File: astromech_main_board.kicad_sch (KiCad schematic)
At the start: 75 parts, among them IC1 MAX11645EUA+, J1 Screw_Terminal_01x02, J10 MOT_HEAD, J11 MOT_RIGHT, J12 RC UART RX, J13 MOT_LEFT, J14 Qwiic, J15 Qwiic, J2 Screw_Terminal_01x02, J3 Screw_Terminal_01x02, J4 IO_XPAND, J5 LEDs, J6 SCREEN, J7 DPAD, J8 RST_BTN, J9 I2C, U1 TCA9554DW, U10 LS7366R, U11 LS7366R, U2 TCA9554DW, U3 NCP1117-3.3_SOT223, U4 NCP1117-5.0_TO252, U5 TXB0108PW, U6 TXB0108PW, U7 TCA9517ADGK, U8 74HC14, U9 LS7366R, Y1 Crystal

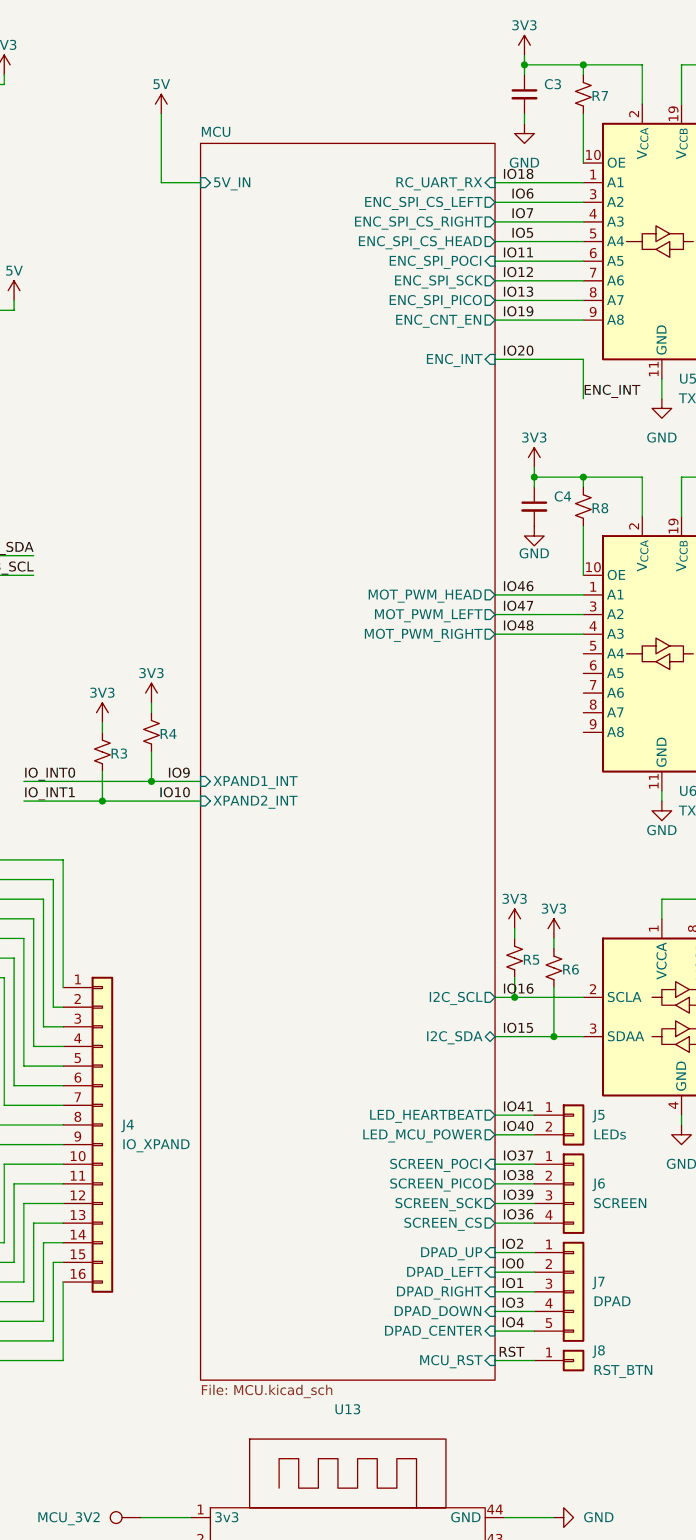
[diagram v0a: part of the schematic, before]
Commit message: Removed Block
- Everything should be on page
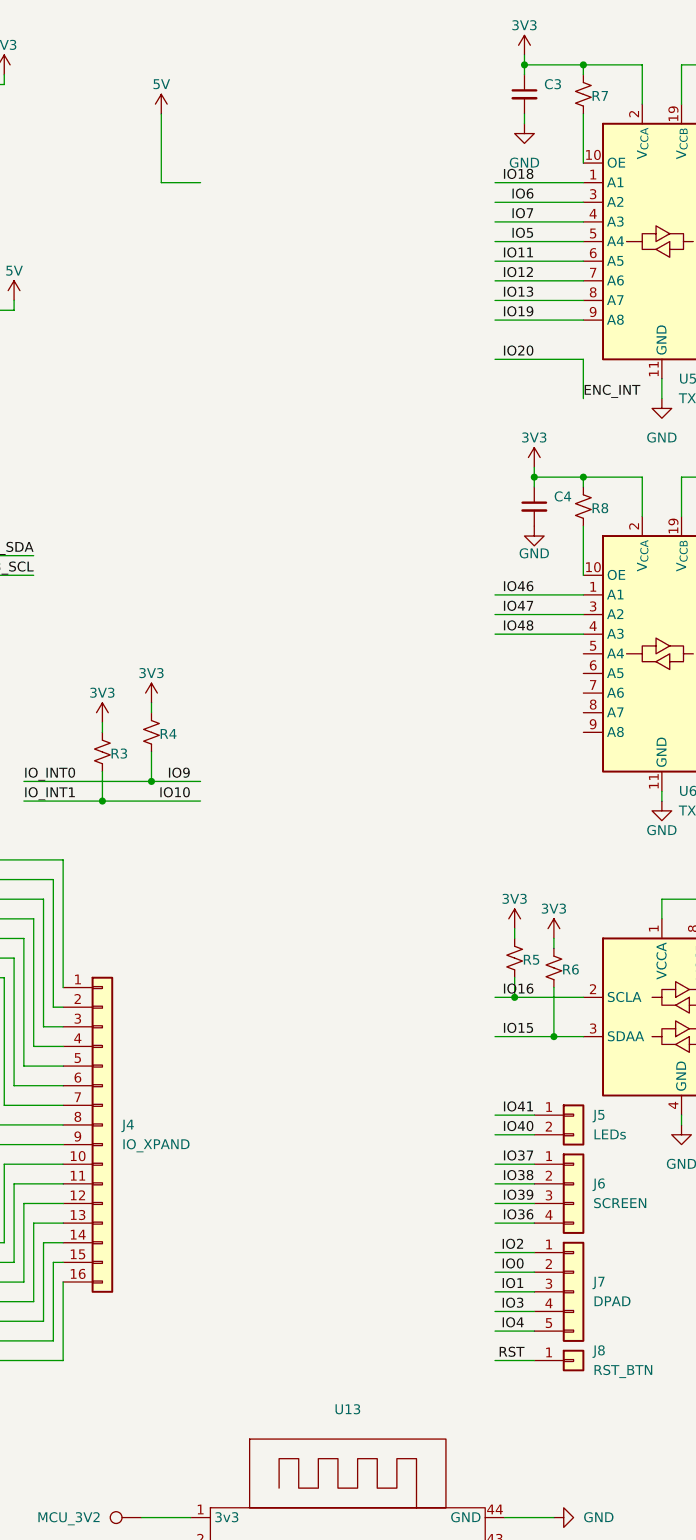
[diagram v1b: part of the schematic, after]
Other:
- removed sheet MCU

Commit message: some board done
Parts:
- removed C3, C5: C_Small, Capacitor_SMD:C_1206_3216Metric, symbol Device:C_Small
- removed J10: MOT_HEAD, Connector_PinHeader_2.54mm:PinHeader_1x04_P2.54mm_Vertical, symbol Connector_Generic:Conn_01x04
- removed J11: MOT_RIGHT, Connector_PinHeader_2.54mm:PinHeader_1x04_P2.54mm_Vertical, symbol Connector_Generic:Conn_01x04
- removed J12: RC UART RX, Connector_PinHeader_2.54mm:PinHeader_1x01_P2.54mm_Vertical, symbol Connector_Generic:Conn_01x01
- removed J13: MOT_LEFT, Connector_PinHeader_2.54mm:PinHeader_1x04_P2.54mm_Vertical, symbol Connector_Generic:Conn_01x04
- removed J15: Qwiic, symbol Connector_Generic:Conn_01x04
- removed J5: LEDs, Connector_PinHeader_2.54mm:PinHeader_1x02_P2.54mm_Vertical, symbol Connector_Generic:Conn_01x02
- removed J6: SCREEN, Connector_PinHeader_2.54mm:PinHeader_1x04_P2.54mm_Vertical, symbol Connector_Generic:Conn_01x04
- removed J7: DPAD, Connector_PinHeader_2.54mm:PinHeader_1x05_P2.54mm_Vertical, symbol Connector_Generic:Conn_01x05
- removed J8: RST_BTN, Connector_PinHeader_2.54mm:PinHeader_1x01_P2.54mm_Vertical, symbol Connector_Generic:Conn_01x01
- removed J9: I2C, Connector_PinHeader_2.54mm:PinHeader_1x02_P2.54mm_Vertical, symbol Connector_Generic:Conn_01x02
- removed JP1, JP2, JP3, JP4, JP5, JP6: SolderJumper_3_Open, Jumper:SolderJumper-3_P1.3mm_Open_RoundedPad1.0x1.5mm, symbol Jumper:SolderJumper_3_Open
- removed JP10, JP11, JP12, JP9: SolderJumper_2_Bridged, Jumper:SolderJumper-2_P1.3mm_Bridged_RoundedPad1.0x1.5mm, symbol Jumper:SolderJumper_2_Bridged
- removed MCU_IO10, MCU_IO11, MCU_IO12, MCU_IO13, MCU_IO14, MCU_IO8, MCU_IO9, MCU_RX2, MCU_TX2: TestPoint, TestPoint:TestPoint_Pad_D1.0mm, symbol Connector:TestPoint
- removed U5: TXB0108PW, Package_SO:TSSOP-20_4.4x6.5mm_P0.65mm, symbol Logic_LevelTranslator:TXB0108PW
- added H1, H2, H3, H4: MountingHole, MountingHole:MountingHole_3.2mm_M3, symbol Mechanical:MountingHole
- added J10: Conn_01x05, astromech_footprints:691210910005, symbol Connector_Generic:Conn_01x05
- added J11, J9: Conn_01x06, astromech_footprints:CONN_SM04B-SRSS-TB_JST, symbol Connector_Generic:Conn_01x06
- added J12, J19, J20, J21: Conn_01x04, astromech_footprints:691210910004, symbol Connector_Generic:Conn_01x04
- added J5, J6: Conn_01x06, astromech_footprints:691210910006, symbol Connector_Generic:Conn_01x06
- added J7: Conn_01x07, Connector_PinSocket_2.54mm:PinSocket_1x07_P2.54mm_Vertical, symbol Connector_Generic:Conn_01x07
- added J8: Conn_01x03, Connector_PinSocket_2.54mm:PinSocket_1x03_P2.54mm_Vertical, symbol Connector_Generic:Conn_01x03
- added R16, R17: R_Small_US, Resistor_SMD:R_1206_3216Metric, symbol Device:R_Small_US
- added unit 5 of U8
- added unit 3 of U8
- added unit 6 of U8
- added unit 4 of U8
- F1, F2: footprint Fuse:FuseHolder_Blade_ATO_Littelfuse_FLR_178.6165 -> Fuse:Fuseholder_Blade_Mini_Keystone_3568
- J1, J2, J3: footprint Connector_PinHeader_2.54mm:PinHeader_1x02_P2.54mm_Vertical -> astromech_footprints:PHOENIX_1984617
- J14: value Qwiic -> Conn_01x04; footprint (none) -> astromech_footprints:691210910004
- J4: footprint Connector_PinHeader_2.54mm:PinHeader_1x16_P2.54mm_Vertical -> astromech_footprints:CUI_TBL009V-254-16GY-2GY
- U8: footprint Package_DIP:DIP-14_W7.62mm -> astromech_footprints:SOIC127P600X175-14N
- Y1: footprint Crystal:Crystal_HC49-4H_Vertical -> Crystal:Crystal_SMD_HC49-SD_HandSoldering
- renumbered MCU_3V2 to MCU_3V3
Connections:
- net IO15 is gone; now on net I2C_3V3_SDA: R6.2, U13.8 (IO_15), U7.3 (SDAA)
- net IO16 is gone; now on net I2C_3V3_SCL: R5.2, U13.9 (IO_16), U7.2 (SCLA)
- net IO19 is gone; now on net ENC_CNT_EN: U13.25 (IO_19)
- net SPI_5V_CIPO is gone; now on net IO11: U10.6 (MISO), U11.6 (MISO), U9.6 (MISO)
- net SPI_5V_COPI is gone; now on net IO13: U10.7 (MOSI), U11.7 (MOSI), U9.7 (MOSI)
- net SPI_5V_CS_HEAD is gone; now on net IO6: U9.4 (SS/)
- net SPI_5V_CS_LEFT is gone; now on net IO5: U10.4 (SS/)
- net SPI_5V_CS_RIGHT is gone; now on net IO7: U11.4 (SS/)
- net SPI_5V_SCK is gone; now on net IO12: U10.5 (SCK), U11.5 (SCK), U9.5 (SCK)
- net 3V3: now also J14.1 (Pin_1), U2.1 (A0), U8.14 (VCC), J10.2 (Pin_2), J11.3 (Pin_3), J5.1 (Pin_1), J9.3 (Pin_3); no longer J14.2 (Pin_2)
- net 5V: now also U13.21 (5Vin), J10.1 (Pin_1), J8.1 (Pin_1); no longer U8.14 (VCC)
- net 5V_IN: no longer U13.21 (5Vin)
- net ENC_INT: now also R7.2
- net GND: now also J14.4 (Pin_4), U1.1 (A0), U1.2 (A1), U1.3 (A2), U2.2 (A1), U2.3 (A2), J10.5 (Pin_5), J11.4 (Pin_4), J12.4 (Pin_4), J19.4 (Pin_4), J20.4 (Pin_4), J21.4 (Pin_4), J5.6 (Pin_6), J6.6 (Pin_6), J8.3 (Pin_3), J9.4 (Pin_4); no longer J14.1 (Pin_1)
- net HEAD_A: now also J19.2 (Pin_2)
- net HEAD_B: now also J19.3 (Pin_3)
- net IO0: now also J6.2 (Pin_2)
- net IO1: now also J6.3 (Pin_3)
- net IO14: now also J7.1 (Pin_1)
- net IO17: now also J14.2 (Pin_2)
- net IO18: now also JP13.1 (A), U8.4
- net IO2: now also J6.1 (Pin_1)
- net IO21: now also J7.2 (Pin_2)
- net IO3: now also J6.4 (Pin_4)
- net IO35: now also J7.3 (Pin_3)
- net IO36: now also J5.5 (Pin_5)
- net IO37: now also J5.2 (Pin_2)
- net IO38: now also J5.3 (Pin_3)
- net IO39: now also J5.4 (Pin_4)
- net IO4: now also J6.5 (Pin_5)
- net IO40: now also J7.4 (Pin_4), R17.1
- net IO41: now also R16.1
- net IO45: now also J7.5 (Pin_5)
- net IO46: now also J19.1 (Pin_1); no longer U6.1 (A1)
- net IO47: now also J20.1 (Pin_1); no longer U6.3 (A2)
- net IO48: now also J21.1 (Pin_1); no longer U6.4 (A3)
- net IO8: now also J14.3 (Pin_3)
- net LEFT_A: now also J20.2 (Pin_2)
- net LEFT_B: now also J20.3 (Pin_3)
- net RIGHT_A: now also J21.2 (Pin_2)
- net RIGHT_B: now also J21.3 (Pin_3)
- net RST: now also J12.3 (Pin_3)
- net SDA_BUFD: now reaches R10.2, U7.6 (SDAB)
- net SDA_BUFD: now also J10.4 (Pin_4), J11.2 (Pin_2), J9.2 (Pin_2)
- net SCL_BUFD: now reaches R9.2, U7.7 (SCLB)
- net SCL_BUFD: now also J10.3 (Pin_3), J11.1 (Pin_1), J9.1 (Pin_1); no longer J14.3 (Pin_3), J14.4 (Pin_4)
- net at U8.2: now also U10.2 (FCKI), U11.2 (FCKI)
- net IORX: now reaches U13.42 (RX)
- net IORX: now also J7.7 (Pin_7)
- net at C7.2, R12.1, Y1.2: now also U9.2 (FCKI)
- net at C8.2, R12.2, U8.1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: now also U9.1 (FCKO)
- net at JP13.2 (C): now also U6.1 (A1)
- net IOTX: now reaches U13.43 (TX)
- net IOTX: now also J7.6 (Pin_6)
- net HEAD_INDEX: no longer names the net of U9.10 (INDEX/)
- net LEFT_INDEX: no longer names the net of U10.10 (INDEX/)
- net PWM_HEAD renamed RC_UART_5V
- net RC_UART_5V: now also J8.2 (Pin_2)
- net PWM_LEFT: no longer names the net of U6.18 (B2)
- net PWM_RIGHT: no longer names the net of U6.17 (B3)
- net RIGHT_INDEX: no longer names the net of U11.10 (INDEX/)
- new net: J12.1 (Pin_1), R16.2
- new net: J12.2 (Pin_2), R17.2
- no-connect marks 6 -> 23
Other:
- note added: "DPAD"
- note added: "Head Motor/Encoder"
- note added: "I2C (3v3 logic level)"
- note added: "I2C Address: 0100000"
- note added: "I2C Address: 0100001"
- note added: "I2C Address: 0110110"
- note added: "Left Motor/Encoder"
- note added: "Net ties (These are artifacts from when the ESP was in a hierarchical sheet)"
- note added: "Qwiic"
- note added: "RC Receiver"
- note added: "Reset Button"
- note added: "Right Motor/Encoder"
- note added: "SOUND UART RX"
- note added: "SOUND UART TX"
- note added: "Screen"
- note added: "Sound UART"
- note added: "Unused"
- note added: "Unused IO"
- moved on the sheet: C4, C6, R3, R4, R8, U6

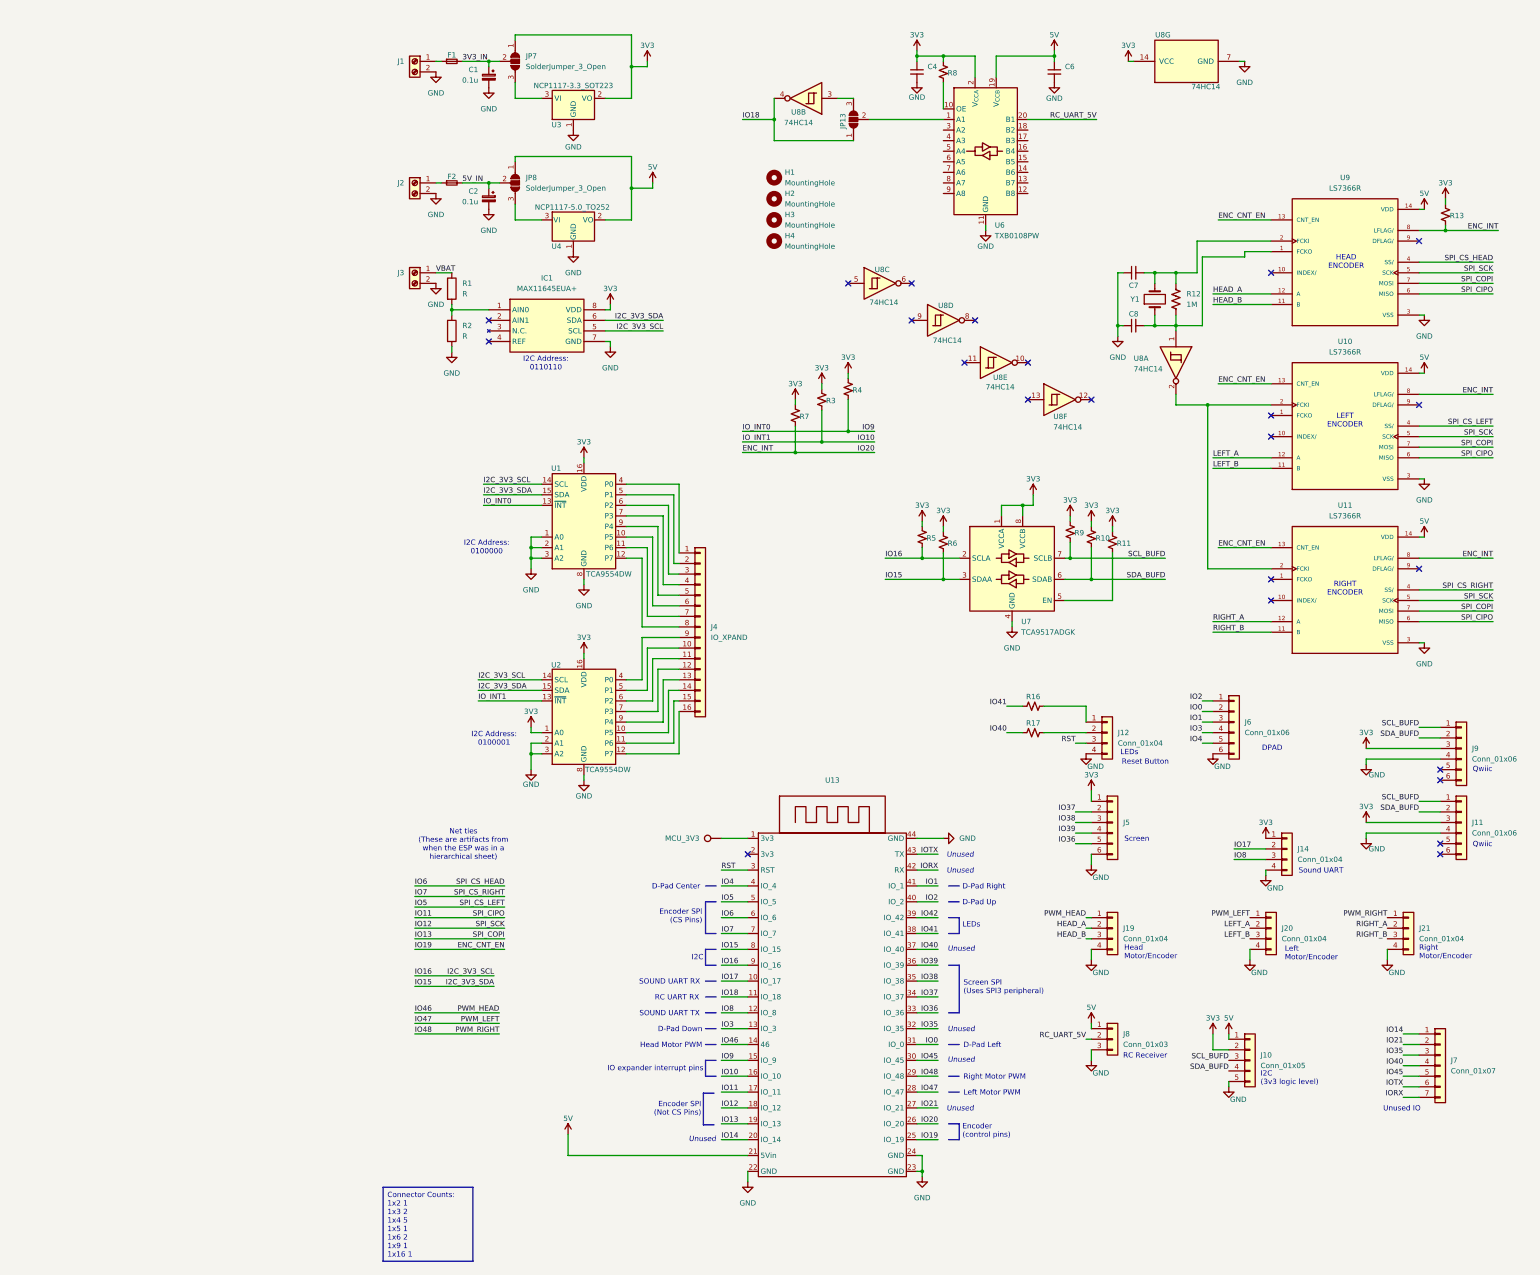
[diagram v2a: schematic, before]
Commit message: added UART chip
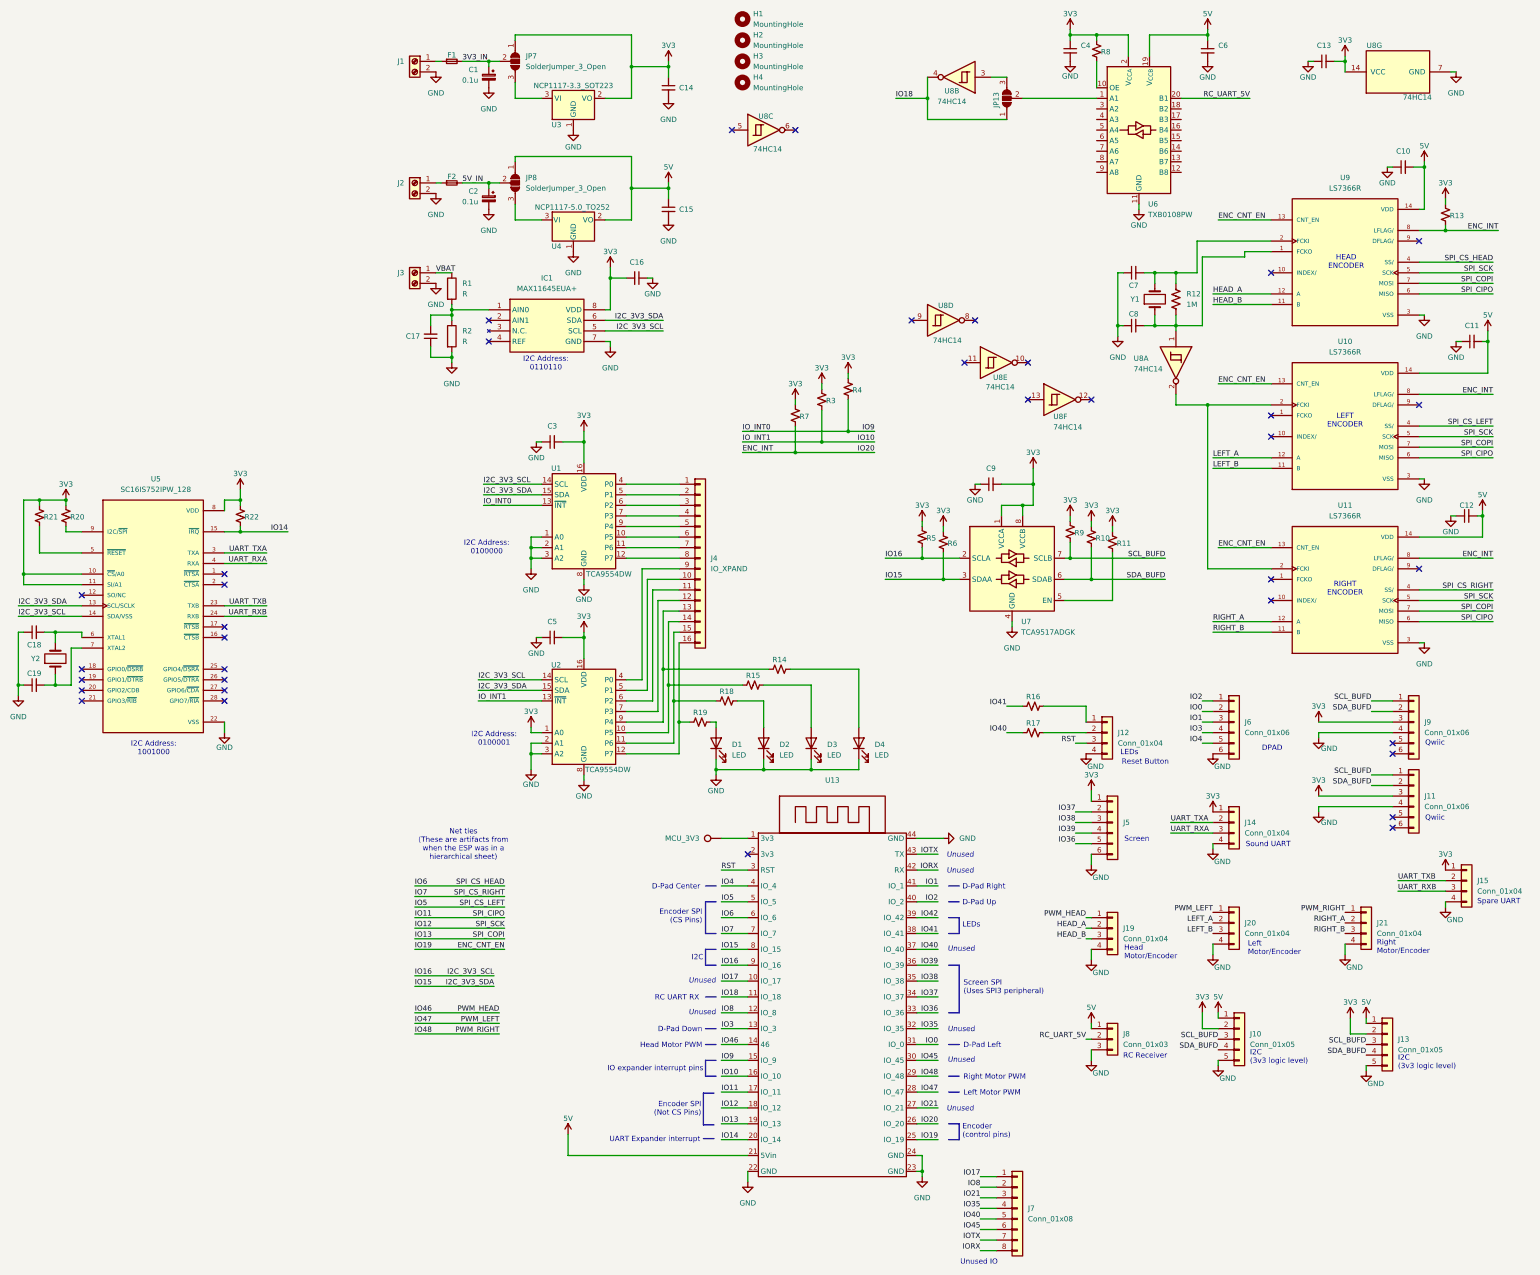
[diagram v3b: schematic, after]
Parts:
- removed J7: Conn_01x07, Connector_PinSocket_2.54mm:PinSocket_1x07_P2.54mm_Vertical, symbol Connector_Generic:Conn_01x07
- added C10, C11, C12, C13, C14, C15, C16, C17, C18, C19, C3, C5, C9: C_Small, Capacitor_SMD:C_1206_3216Metric, symbol Device:C_Small
- added D1, D2, D3, D4: LED, LED_SMD:LED_1206_3216Metric_Pad1.42x1.75mm_HandSolder, symbol Device:LED
- added J13: Conn_01x05, astromech_footprints:691210910005, symbol Connector_Generic:Conn_01x05
- added J15: Conn_01x04, astromech_footprints:691210910004, symbol Connector_Generic:Conn_01x04
- added J7: Conn_01x08, Connector_PinHeader_2.54mm:PinHeader_1x08_P2.54mm_Vertical, symbol Connector_Generic:Conn_01x08
- added R14, R15, R18, R19, R20, R21, R22: R_Small_US, Resistor_SMD:R_1206_3216Metric, symbol Device:R_Small_US
- added U5: SC16IS752IPW_128, astromech_footprints:SOP65P640X110-28N, symbol astromech_symbols:SC16IS752IPW_128
- added Y2: Crystal, Crystal:Crystal_SMD_HC49-SD_HandSoldering, symbol Device:Crystal
- C1, C2: footprint Capacitor_SMD:C_1206_3216Metric -> Capacitor_SMD:CP_Elec_6.3x5.8
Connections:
- net 3V3: now also C13.2, C14.1, C16.2, C3.2, C5.2, C9.2, J13.2 (Pin_2), J15.1 (Pin_1), R20.1, R21.1, R22.1, U5.10 (~{CS}/A0), U5.11 (SI/A1), U5.8 (VDD)
- net 5V: now also C10.2, C11.2, C12.2, C15.1, J13.1 (Pin_1)
- net GND: now also C10.1, C11.1, C12.1, C13.1, C14.2, C15.2, C16.1, C17.1, C18.1, C19.1, C3.1, C5.1, C9.1, D1.1 (K), D2.1 (K), D3.1 (K), D4.1 (K), J13.5 (Pin_5), J15.4 (Pin_4), U5.22 (VSS)
- net I2C_3V3_SCL: now also U5.14 (SDA/VSS)
- net I2C_3V3_SDA: now also U5.13 (SCL/SCLK)
- net IO14: now also R22.2, U5.15 (~{IRQ})
- net IO17: now also J7.1 (Pin_1); no longer J14.2 (Pin_2)
- net IO21: now also J7.3 (Pin_3)
- net IO35: now also J7.4 (Pin_4)
- net IO40: now also J7.5 (Pin_5)
- net IO45: now also J7.6 (Pin_6)
- net IO8: now also J7.2 (Pin_2); no longer J14.3 (Pin_3)
- net IORX: now also J7.8 (Pin_8)
- net IOTX: now also J7.7 (Pin_7)
- net SCL_BUFD: now also J13.3 (Pin_3)
- net SDA_BUFD: now also J13.4 (Pin_4)
- net at IC1.1 (AIN0), R1.2, R2.1: now also C17.2
- net at J4.14 (Pin_14), U2.10 (P5): now also R15.1
- net at J4.15 (Pin_15), U2.11 (P6): now also R18.1
- net at J4.16 (Pin_16), U2.12 (P7): now also R19.1
- net at J4.13 (Pin_13), U2.9 (P4): now also R14.1
- new net: D4.2 (A), R14.2
- new net: C19.2, U5.7 (XTAL2), Y2.1
- new net: C18.2, U5.6 (XTAL1), Y2.2
- new net: R21.2, U5.5 (~{RESET})
- new net: R20.2, U5.9 (I2C/~{SPI})
- new net: D1.2 (A), R19.2
- new net: D3.2 (A), R15.2
- new net: D2.2 (A), R18.2
- new net UART_RXA: J14.3 (Pin_3), U5.4 (RXA)
- new net UART_RXB: J15.3 (Pin_3), U5.24 (RXB)
- new net UART_TXA: J14.2 (Pin_2), U5.3 (TXA)
- new net UART_TXB: J15.2 (Pin_2), U5.23 (TXB)
- no-connect marks 23 -> 36
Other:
- note added: "I2C Address: 1001000"
- note added: "Spare UART"
- note added: "UART Expander interrupt"
- note removed: "SOUND UART RX"
- note removed: "SOUND UART TX"
- moved on the sheet: C4, C6, H1, H2, H3, H4, J10, J11, J14, J20, J21, J4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
